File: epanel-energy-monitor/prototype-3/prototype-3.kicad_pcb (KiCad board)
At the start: 2 copper layers, 87 x 68 mm, 31 parts, among them J1 Screw_Terminal_01x02, J10 Conn_01x02_Male, J2 Conn_01x03_Male, J3 Conn_01x01_Male, J4 Conn_01x01_Male, J5 Conn_01x01, J6 Conn_02x05, J7 Conn_02x05, J8 AudioJack4, J9 Screw_Terminal_01x02, Q1 CJ2302, U1 ESP32-POE, U2 MCP3208, U3 LTV-814

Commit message: wip pcb
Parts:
- added C1: 1uF/6V, Resistor_SMD:R_0603_1608Metric, F.Cu at (72.3, 85.3)
- added C2: 10uF/6V, Resistor_SMD:R_0603_1608Metric, F.Cu at (68.3, 89.7)
- added C4: 10uF/6V, Resistor_SMD:R_0603_1608Metric, F.Cu at (91.8, 68.4)
- added C5: 10uF/6V, Resistor_SMD:R_0603_1608Metric, F.Cu at (79.9, 75.7)
- added D1: LED, Diode_SMD:D_0805_2012Metric, F.Cu at (80.2, 73.0)
- added J12: Conn_01x03_Male, Connector_PinHeader_2.54mm:PinHeader_1x03_P2.54mm_Vertical, F.Cu at (68.4, 73.1)
- added J13: Conn_01x03_Male, Connector_PinHeader_2.54mm:PinHeader_1x03_P2.54mm_Vertical, F.Cu at (75.6, 64.1)
- added J15: Conn_02x05, Connector_PinHeader_2.54mm:PinHeader_2x05_P2.54mm_Vertical, F.Cu at (31.0, 89.2)
- added J16: Conn_02x05, Connector_PinHeader_2.54mm:PinHeader_2x05_P2.54mm_Vertical, F.Cu at (56.8, 64.1)
- added J17: Screw_Terminal_01x02, TerminalBlock:TerminalBlock_bornier-2_P5.08mm, F.Cu at (57.7, 81.1)
- added J18: Screw_Terminal_01x02, TerminalBlock:TerminalBlock_bornier-2_P5.08mm, F.Cu at (64.9, 66.3)
- added J19: Screw_Terminal_01x02, TerminalBlock:TerminalBlock_bornier-2_P5.08mm, F.Cu at (39.1, 91.4)
- added J6: Conn_02x03, Connector_PinHeader_2.54mm:PinHeader_2x03_P2.54mm_Vertical, F.Cu at (84.9, 64.1)
- added J9: Conn_02x03, Connector_PinHeader_2.54mm:PinHeader_2x03_P2.54mm_Vertical, F.Cu at (73.0, 73.8)
- added R1: 1KΩ, Resistor_SMD:R_0603_1608Metric, F.Cu at (63.7, 74.5)
- added R11: 470KΩ, Resistor_SMD:R_0603_1608Metric, F.Cu at (91.8, 65.9)
- added R17: 1KΩ, Resistor_SMD:R_0603_1608Metric, F.Cu at (72.3, 87.8)
- added R18: 1KΩ, Resistor_SMD:R_0603_1608Metric, F.Cu at (58.8, 99.5)
- added R19: 100KΩ, Resistor_SMD:R_0603_1608Metric, F.Cu at (68.3, 92.2)
- added R20: 12KΩ, Resistor_SMD:R_0603_1608Metric, F.Cu at (63.7, 72.0)
- added R26: 200Ω/0.5W, Resistor_SMD:R_0805_2012Metric, F.Cu at (54.6, 99.7)
- added R27: 120Ω/0.5W, Resistor_SMD:R_0805_2012Metric, F.Cu at (68.3, 82.0)
- added R28: 100Ω/0.5W, Resistor_SMD:R_0805_2012Metric, F.Cu at (50.2, 98.0)
- added R29: 62Ω/0.5W, Resistor_SMD:R_0805_2012Metric, F.Cu at (84.6, 72.9)
- added R30: 33Ω/0.5W, Resistor_SMD:R_0805_2012Metric, F.Cu at (92.0, 63.2)
- added R31: 200Ω/0.5W, Resistor_SMD:R_0805_2012Metric, F.Cu at (64.1, 87.1)
- added R32: 120Ω/0.5W, Resistor_SMD:R_0805_2012Metric, F.Cu at (56.9, 96.8)
- added R33: 100Ω/0.5W, Resistor_SMD:R_0805_2012Metric, F.Cu at (64.1, 90.0)
- added R34: 62Ω/0.5W, Resistor_SMD:R_0805_2012Metric, F.Cu at (72.7, 82.6)
- added R35: 33Ω/0.5W, Resistor_SMD:R_0805_2012Metric, F.Cu at (64.1, 93.0)
- added R5: 12KΩ, Resistor_SMD:R_0603_1608Metric, F.Cu at (68.3, 87.2)
- added R6: 12KΩ, Resistor_SMD:R_0603_1608Metric, F.Cu at (96.2, 63.0)
- added R7: 470KΩ, Resistor_SMD:R_0603_1608Metric, F.Cu at (88.8, 72.7)
- added R8: 470KΩ, Resistor_SMD:R_0603_1608Metric, F.Cu at (68.3, 84.7)
- added T1: 230V - 6V, mylife-footprints:RS PRO 6V 0.35VA, F.Cu at (34.1, 66.8)
- added U4: ADS1115, Package_SO:TSSOP-10_3x3mm_P0.5mm, F.Cu at (39.4, 98.2)
- added U5: LMV321, Package_TO_SOT_SMD:SOT-23-5, F.Cu at (45.4, 98.8)
- J10: value Conn_01x02_Male -> Conn_01x03_Male; footprint Connector_PinHeader_2.54mm:PinHeader_1x02_P2.54mm_Vertical -> Connector_PinHeader_2.54mm:PinHeader_1x03_P2.54mm_Vertical
- J7: value Conn_02x05 -> Conn_02x03; footprint Connector_PinHeader_2.54mm:PinHeader_2x05_P2.54mm_Vertical -> Connector_PinHeader_2.54mm:PinHeader_2x03_P2.54mm_Vertical
- J8: value AudioJack4 -> Conn_02x03; footprint Connector_Audio:Jack_3.5mm_PJ320D_Horizontal -> Connector_PinHeader_2.54mm:PinHeader_2x03_P2.54mm_Vertical
- Q1: value CJ2302 -> BSS138
- R12: value 1.2KΩ -> 470KΩ
- R13: value 2KΩ -> 470KΩ
- R14: value 3.3KΩ -> 470KΩ
- R15: value 4.7KΩ -> 1KΩ
- R21: renamed from R6; value 220Ω/0.5W -> 200Ω/0.5W
- R22: renamed from R7; value 150Ω/0.5W -> 120Ω/0.5W
- R23: renamed from R8; value 120Ω/0.5W -> 100Ω/0.5W
- R24: renamed from R9; value 75Ω/0.5W -> 62Ω/0.5W
- R3: renamed from R5; value 10KΩ -> 3.3KΩ
- R4: renamed from R11; value 1KΩ -> 220Ω
- moved J8 130.6 mm to (57.0, 87.9), turned to 0 degrees
- moved J7 122.8 mm to (49.8, 89.2)
- moved R15 122.0 mm to (61.1, 96.5), turned to 0 degrees
- moved R13 104.5 mm to (76.9, 82.4), turned to 0 degrees
- moved R14 100.3 mm to (79.9, 78.2), turned to 0 degrees
- moved J10 96.6 mm to (80.2, 64.1)
- moved R12 96.3 mm to (84.4, 75.6), turned to 0 degrees
- renumbered C1 to C3, J3 to J1, J2 to J11, J6 to J14, J4 to J2, J1 to J3, J5 to J4, J9 to J5, R2 to R10, R4 to R16, R3 to R2, R10 to R25, R1 to R9, U3 to U2, U2 to U3
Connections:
- C3 pad 1: Net-(C1-Pad1) -> Net-(C3-Pad1)
- J1 pad 1: Net-(J3-Pad1) -> Net-(J1-Pad1)
- J10 pad 1: Net-(J10-Pad1) -> Net-(C2-Pad1)
- J10 pad 2: Net-(C1-Pad1) -> Net-(J10-Pad2)
- J11 pad 1: Net-(J2-Pad1) -> Net-(C3-Pad1)
- J11 pad 2: Net-(J2-Pad2) -> Net-(J11-Pad2)
- J11 pad 3: Net-(J2-Pad3) -> Net-(J10-Pad3)
- J14 pad 1: Net-(C1-Pad1) -> Net-(J11-Pad2)
- J14 pad 3: Net-(C1-Pad1) -> Net-(J11-Pad2)
- J14 pad 5: Net-(C1-Pad1) -> Net-(J11-Pad2)
- J14 pad 7: Net-(C1-Pad1) -> Net-(J11-Pad2)
- J14 pad 9: Net-(C1-Pad1) -> Net-(J11-Pad2)
- J5 pad 1: Net-(J9-Pad1) -> Net-(J5-Pad1)
- J7 pad 3: Net-(J7-Pad1) -> Net-(J7-Pad3)
- J7 pad 4: Net-(J7-Pad4) -> Net-(J7-Pad2)
- J7 pad 5: Net-(J7-Pad1) -> Net-(J7-Pad5)
- J7 pad 6: Net-(J7-Pad6) -> Net-(J7-Pad2)
- Q1 pad 1: Net-(J3-Pad1) -> Net-(J1-Pad1)
- R10 pad 2: Net-(C1-Pad1) -> Net-(C3-Pad1)
- R12 pad 1: Net-(J9-Pad1) -> GND
- R12 pad 2: Net-(J7-Pad4) -> Net-(C4-Pad1)
- R13 pad 1: Net-(J9-Pad1) -> Net-(C5-Pad1)
- R13 pad 2: Net-(J7-Pad6) -> +3V3
- R14 pad 1: Net-(J9-Pad1) -> GND
- R14 pad 2: Net-(J7-Pad8) -> Net-(C5-Pad1)
- R15 pad 1: Net-(J9-Pad1) -> Net-(J6-Pad2)
- R15 pad 2: Net-(J7-Pad10) -> Net-(R15-Pad2)
- R16 pad 1: Net-(J2-Pad2) -> Net-(J7-Pad2)
- R16 pad 2: Net-(J10-Pad1) -> Net-(J17-Pad1)
- R2 pad 1: Net-(J3-Pad1) -> Net-(J1-Pad1)
- R21 pad 1: Net-(J10-Pad1) -> Net-(J17-Pad1)
- R22 pad 1: Net-(J10-Pad1) -> Net-(J17-Pad1)
- R23 pad 1: Net-(J10-Pad1) -> Net-(J17-Pad1)
- R24 pad 1: Net-(J10-Pad1) -> Net-(J17-Pad1)
- R25 pad 1: Net-(J10-Pad1) -> Net-(J17-Pad1)
- R4 pad 1: Net-(J9-Pad1) -> Net-(J5-Pad1)
- R4 pad 2: Net-(J7-Pad2) -> Net-(R4-Pad2)
- R9 pad 1: Net-(C1-Pad1) -> Net-(C3-Pad1)
- U1 pad 14: unconnected-(U1-Pad14) -> Net-(U1-Pad14)
- U1 pad 15: Net-(J2-Pad1) -> Net-(J7-Pad1)
- U1 pad 16: Net-(U1-Pad16) -> Net-(J6-Pad1)
- U1 pad 18: unconnected-(U1-Pad18) -> Net-(U1-Pad18)
- U1 pad 19: unconnected-(U1-Pad19) -> Net-(U1-Pad19)
- U1 pad 7: unconnected-(U1-Pad7) -> Net-(J1-Pad1)
- U1 pad 8: Net-(J3-Pad1) -> unconnected-(U1-Pad8)
- U2 pad 1: Net-(J7-Pad1) -> Net-(R4-Pad2)
- U3 pad 1: Net-(J2-Pad3) -> Net-(J6-Pad5)
- U3 pad 10: Net-(U1-Pad16) -> Net-(U1-Pad14)
- U3 pad 2: unconnected-(U2-Pad2) -> Net-(J7-Pad5)
- U3 pad 3: unconnected-(U2-Pad3) -> Net-(J8-Pad5)
- U3 pad 4: unconnected-(U2-Pad4) -> Net-(J9-Pad5)
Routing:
- net Net-(J2-Pad1): track 54.7 -> 0.00 mm
- net Net-(C3-Pad1): track 0.00 -> 54.7 mm
- net Net-(J17-Pad1): track 0.00 -> 44.1 mm, vias 0 -> 1
- net Net-(J10-Pad1): track 44.1 -> 0.00 mm, vias 1 -> 0
- net Net-(U1-Pad16): track 42.8 -> 0.00 mm, vias 1 -> 0
- net Net-(U1-Pad14): track 0.00 -> 42.8 mm, vias 0 -> 1
- net Net-(J3-Pad1): track 37.9 -> 0.00 mm
- net Net-(J1-Pad1): track 0.00 -> 37.9 mm
- net Net-(J11-Pad2): track 0.00 -> 35.8 mm
- net Net-(C1-Pad1): track 32.5 -> 0.00 mm
- net (no net): track 0.00 -> 31.5 mm
- net Net-(R4-Pad2): track 0.00 -> 23.0 mm
- net Net-(J9-Pad1): track 18.4 -> 0.00 mm
- net Net-(J5-Pad1): track 0.00 -> 18.4 mm
- net Net-(J7-Pad1): track 15.1 -> 0.00 mm
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
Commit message: init pcb
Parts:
- moved R4 165.7 mm to (42.8, 149.2), turned to 0 degrees
- moved Q1 155.7 mm to (29.6, 150.2), turned to 0 degrees
- moved J2 155.6 mm to (34.4, 150.2)
- moved R10 153.3 mm to (38.8, 151.7)
- moved R3 149.7 mm to (38.8, 149.2)
- moved J14 137.6 mm to (55.4, 111.7), turned to 0 degrees
- moved R22 129.0 mm to (62.4, 122.3), turned to 0 degrees
- moved R2 125.4 mm to (55.0, 136.7), turned to 0 degrees
- moved C3 125.2 mm to (59.7, 132.1), turned to 0 degrees
- moved J4 125.1 mm to (55.4, 133.2)
- moved U2 123.5 mm to (58.7, 127.5), turned to 0 degrees
- moved R23 122.2 mm to (66.8, 122.3), turned to 0 degrees
- moved R24 121.0 mm to (66.5, 125.2), turned to 0 degrees
- moved R16 120.6 mm to (66.3, 128.0), turned to 0 degrees
- moved R21 111.6 mm to (80.2, 110.8), turned to 0 degrees
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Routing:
- net GND: track 75.9 -> 0.00 mm
- net +3V3: track 62.9 -> 0.00 mm, vias 4 -> 0
- net +5V: track 62.1 -> 0.00 mm
- net Net-(U1-Pad11): track 59.1 -> 0.00 mm
- net Net-(U1-Pad12): track 58.5 -> 0.00 mm
- net Net-(U1-Pad13): track 58.0 -> 0.00 mm
- net Net-(C3-Pad1): track 54.7 -> 0.00 mm
- net Net-(J17-Pad1): track 44.1 -> 0.00 mm, vias 1 -> 0
- net Net-(U1-Pad14): track 42.8 -> 0.00 mm, vias 1 -> 0
- net Net-(J1-Pad1): track 37.9 -> 0.00 mm
- net Net-(J11-Pad2): track 35.8 -> 0.00 mm
- net Net-(J5-Pad2): track 34.6 -> 0.00 mm, vias 1 -> 0
- net (no net): track 31.5 -> 0.00 mm
- net LINE: track 26.2 -> 0.00 mm
- net NEUT: track 24.8 -> 0.00 mm
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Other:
- board text removed: "1.2KΩ"
- board text removed: "10A"
- board text removed: "16A"
- board text removed: "1KΩ"
- board text removed: "20A"
- board text removed: "2KΩ"
- board text removed: "3.3KΩ"
- board text removed: "32A"
- board text removed: "4.7KΩ"
- board text removed: "60A"

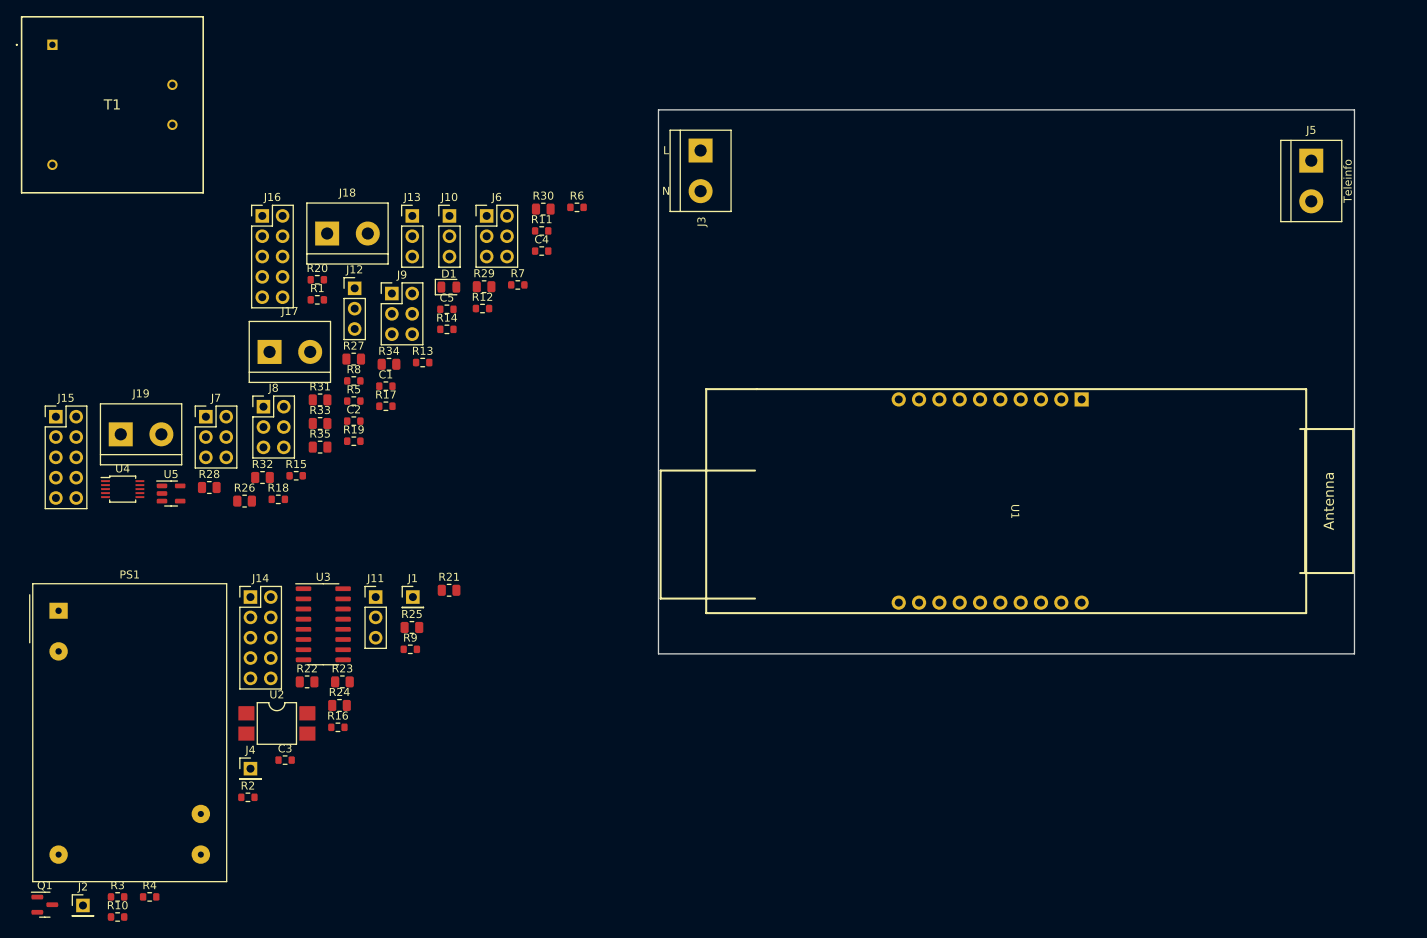
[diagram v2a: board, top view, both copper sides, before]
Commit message: increase board size
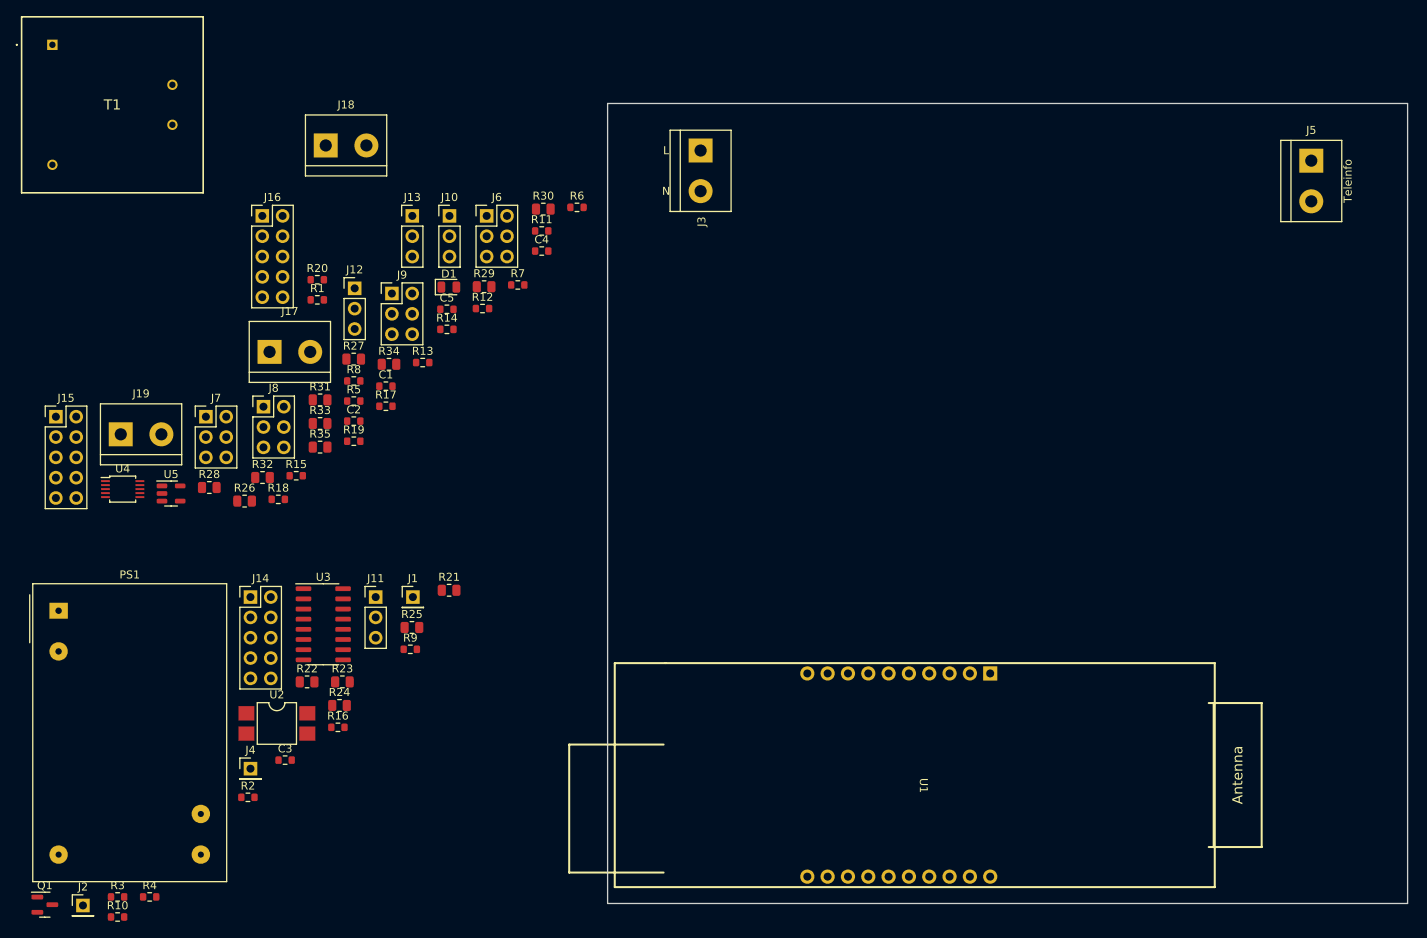
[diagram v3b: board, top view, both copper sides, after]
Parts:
- moved U1 36.1 mm to (137.8, 134.0)
- moved J18 11.0 mm to (64.8, 55.2)
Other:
- board size 87 x 68 mm -> 100 x 100 mm
- board text removed: "Size: 87 x 68"
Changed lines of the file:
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@@
   )
   (footprint "TerminalBlock:TerminalBlock_bornier-2_P5.08mm" (layer "F.Cu")
-    (at 64.945 66.255)
+    (at 64.77 55.245)
     (descr "simple 2-pin terminal block, pitch 5.08mm, revamped version of bornier2")
     (tags "terminal block bornier2")
@@
   )
   (footprint "mylife-footprints:ESP32-POE" (layer "F.Cu")
-    (at 149.225 99.735 -90)
+    (at 137.795 133.985 -90)
     (property "Sheetfile" "prototype-3.kicad_sch")
     (property "Sheetname" "")
@@
     )
   )
-  (gr_line locked (start 106.36 50.8) (end 193.36 50.8) (layer "Edge.Cuts") (width 0.1))
-  (gr_line locked (start 106.36 118.8) (end 106.36 50.8) (layer "Edge.Cuts") (width 0.1))
-  (gr_line locked (start 193.36 118.8) (end 193.36 50.8) (layer "Edge.Cuts") (width 0.1))
-  (gr_line locked (start 106.36 118.8) (end 193.36 118.8) (layer "Edge.Cuts") (width 0.1))
+  (gr_line locked (start 100 50) (end 200 50) (layer "Edge.Cuts") (width 0.1))
+  (gr_line locked (start 100 150) (end 100 50) (layer "Edge.Cuts") (width 0.1))
+  (gr_line locked (start 200 150) (end 200 50) (layer "Edge.Cuts") (width 0.1))
+  (gr_line locked (start 100 150) (end 200 150) (layer "Edge.Cuts") (width 0.1))
   (gr_text "L" (at 107.315 55.88) (layer "F.SilkS")
     (effects (font (size 1 1) (thickness 0.15)))
@@
     (effects (font (size 1 1) (thickness 0.15)))
   )
-  (gr_text "Size: 87 x 68" (at 198.12 172.72) (layer "Cmts.User")
-    (effects (font (size 3 3) (thickness 0.15)))
-  )
 )

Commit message: teleinfo
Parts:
- moved R4 171.3 mm to (188.4, 59.1), turned to 180 degrees
- moved Q1 168.5 mm to (171.4, 59.1), turned to 90 degrees
- moved J2 167.5 mm to (171.4, 54.0)
- moved R3 164.8 mm to (175.9, 57.8)
- moved J19 155.8 mm to (194.9, 91.4), turned to -90 degrees
- moved U2 145.1 mm to (184.2, 54.6), turned to 180 degrees
- moved J4 144.2 mm to (175.9, 54.0)
- moved J17 137.9 mm to (194.9, 67.3), turned to -90 degrees
- moved R2 136.6 mm to (163.2, 53.3), turned to 90 degrees
- moved J18 132.4 mm to (194.9, 79.4), turned to -90 degrees
- moved U4 129.5 mm to (167.6, 116.2)
- moved J1 108.1 mm to (167.0, 54.0)
- moved R1 99.2 mm to (160.7, 53.3), turned to 90 degrees
- moved U3 91.3 mm to (155.6, 109.2)
- moved PS1 89.1 mm to (114.4, 81.3)
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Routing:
- net +3V3: track 0.00 -> 31.2 mm
- net Net-(J4-Pad1): track 0.00 -> 14.4 mm
- net Net-(J1-Pad1): track 0.00 -> 13.9 mm
- net GND: track 0.00 -> 7.90 mm
- net Net-(J5-Pad2): track 0.00 -> 7.25 mm
- net Net-(J5-Pad1): track 0.00 -> 5.72 mm
- net Net-(R4-Pad2): track 0.00 -> 3.33 mm
- net Net-(D1-Pad1): track 0.00 -> 3.27 mm
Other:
- board text added: "CT0"
- board text added: "CT1"
- board text added: "CT2"

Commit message: alim + v-sens
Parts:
- moved C2 86.3 mm to (149.2, 59.7)
- moved R8 85.3 mm to (149.2, 57.8), turned to 180 degrees
- moved R15 83.5 mm to (137.2, 62.2), turned to 90 degrees
- moved R19 76.7 mm to (137.2, 58.4), turned to -90 degrees
- moved R20 75.5 mm to (137.2, 54.6), turned to -90 degrees
- moved R7 62.7 mm to (149.2, 55.9)
- moved J10 62.5 mm to (142.2, 55.9)
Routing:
- net LINE: track 0.00 -> 38.3 mm
- net NEUT: track 0.00 -> 34.5 mm
- net GND: track 7.90 -> 36.5 mm, vias 0 -> 1
- net Net-(J10-Pad2): track 0.00 -> 18.7 mm
- net Net-(R19-Pad2): track 0.00 -> 10.1 mm
- net Net-(C2-Pad1): track 0.00 -> 9.98 mm
- net +3V3: track 31.2 -> 40.8 mm
- net Net-(R15-Pad2): track 0.00 -> 7.39 mm
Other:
- board text added: "DIV"
- board text added: "GND"
- board text added: "LTV"
- board text added: "OP"
- board text added: "OUT"
- board text added: "V-sens"
